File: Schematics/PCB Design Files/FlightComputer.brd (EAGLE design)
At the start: 50.5 x 101.6 mm, 9 parts

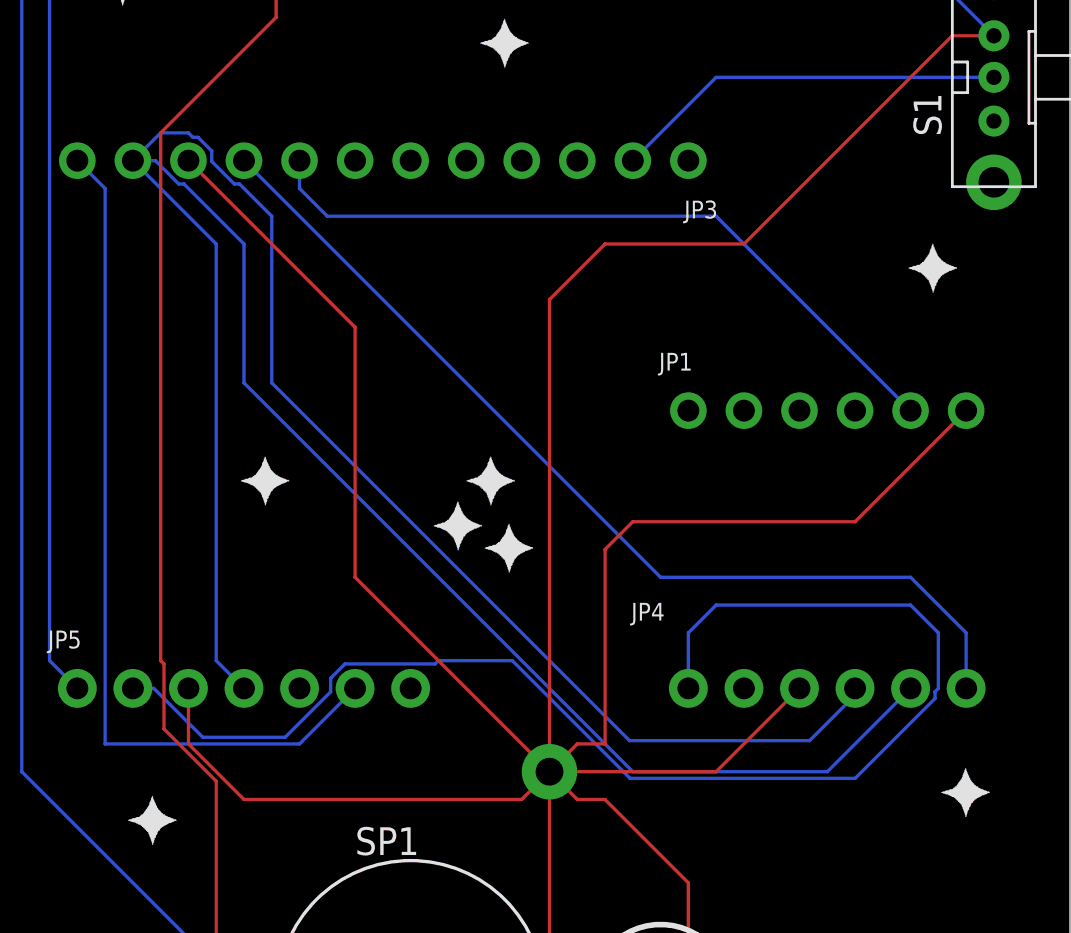
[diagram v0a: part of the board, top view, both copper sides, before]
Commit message: Created header files for simplicity and abstracted code for cleanliness
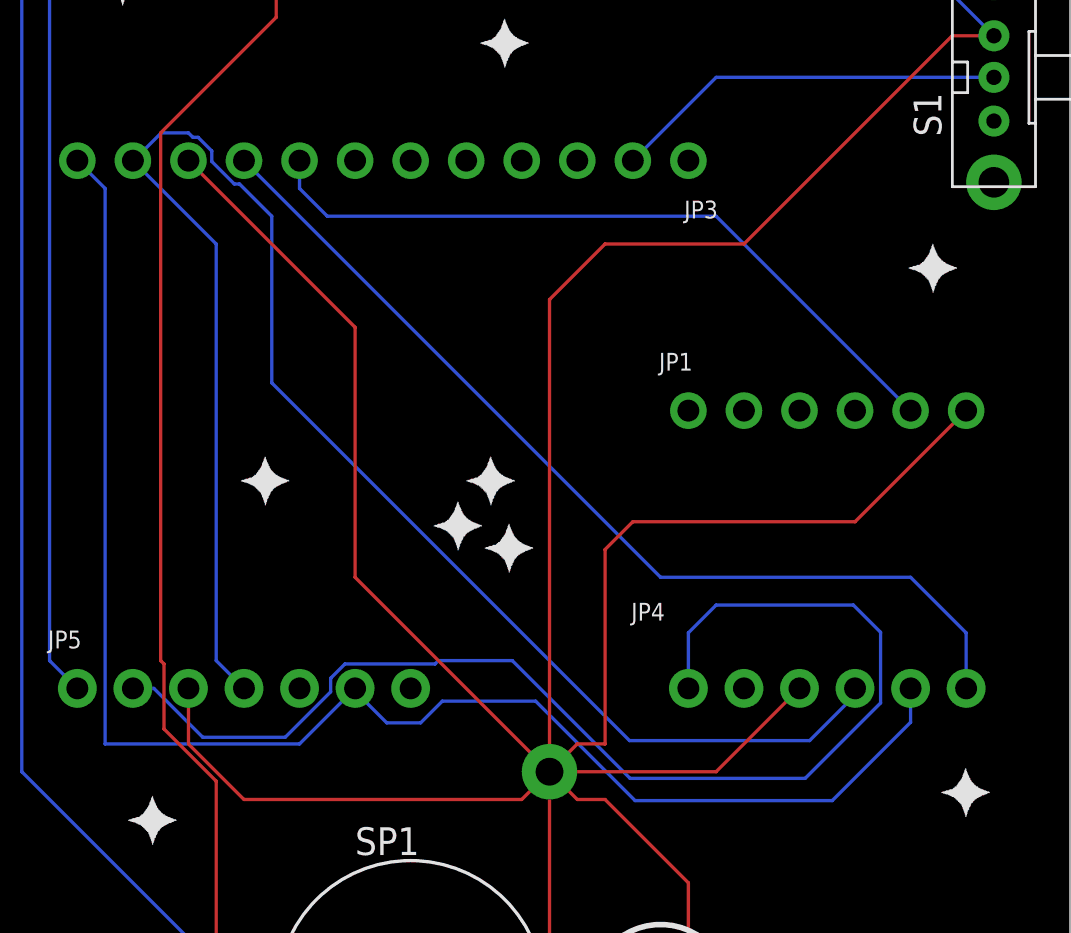
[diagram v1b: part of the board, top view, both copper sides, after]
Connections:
- net SCL: no longer JP4.5
- net SDA: now also JP4.5
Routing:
- net SCL: track 129.6 -> 77.2 mm
- net SDA: track 39.7 -> 71.1 mm
- net 3.3V: track 61.3 -> 56.2 mm
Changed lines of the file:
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@@
 <drawing>
 <settings>
-<setting alwaysvectorfont="yes"/>
+<setting alwaysvectorfont="no"/>
 <setting verticaltext="up"/>
 </settings>
@@
 <contactref element="JP5" pad="4"/>
 <contactref element="JP3" pad="11"/>
-<contactref element="JP4" pad="5"/>
 <wire x1="29.21" y1="57.15" x2="33.02" y2="53.34" width="0.1524" layer="16"/>
 <wire x1="33.02" y1="34.29" x2="34.29" y2="33.02" width="0.1524" layer="16"/>
 <wire x1="33.02" y1="53.34" x2="33.02" y2="34.29" width="0.1524" layer="16"/>
-<wire x1="64.77" y1="33.02" x2="60.96" y2="29.21" width="0.1524" layer="16"/>
-<wire x1="34.29" y1="46.99" x2="34.29" y2="53.34" width="0.1524" layer="16"/>
-<wire x1="34.29" y1="53.34" x2="31.5468" y2="56.0832" width="0.1524" layer="16"/>
-<wire x1="31.5468" y1="56.0832" x2="31.3081125" y2="56.0832" width="0.1524" layer="16"/>
-<wire x1="30.2413125" y1="57.15" x2="29.21" y2="57.15" width="0.1524" layer="16"/>
-<wire x1="31.3081125" y1="56.0832" x2="30.2413125" y2="57.15" width="0.1524" layer="16"/>
-<wire x1="60.96" y1="29.21" x2="52.07" y2="29.21" width="0.1524" layer="16"/>
-<wire x1="52.07" y1="29.21" x2="34.29" y2="46.99" width="0.1524" layer="16"/>
 <wire x1="62.23" y1="33.02" x2="62.23" y2="32.70946875" width="0.1524" layer="16"/>
 <wire x1="62.23" y1="32.70946875" x2="60.15293125" y2="30.6324" width="0.1524" layer="16"/>
@@
 <wire x1="33.8481125" y1="56.0832" x2="32.8168" y2="57.1145125" width="0.1524" layer="16"/>
 <wire x1="32.8168" y1="57.1145125" x2="32.8168" y2="57.5918875" width="0.1524" layer="16"/>
-<wire x1="31.75" y1="58.42" x2="30.48" y2="58.42" width="0.1524" layer="16"/>
-<wire x1="30.48" y1="58.42" x2="29.21" y2="57.15" width="0.1524" layer="16"/>
+<wire x1="31.75" y1="58.42" x2="30.5054" y2="58.42" width="0.1524" layer="16"/>
+<wire x1="30.5054" y1="58.42" x2="29.2354" y2="57.15" width="0.1524" layer="16"/>
+<wire x1="29.2354" y1="57.15" x2="29.21" y2="57.15" width="0.1524" layer="16"/>
 </signal>
 <signal name="SDA">
@@
 <wire x1="27.94" y1="30.48" x2="36.83" y2="30.48" width="0.1524" layer="16"/>
 <wire x1="36.83" y1="30.48" x2="39.37" y2="33.02" width="0.1524" layer="16"/>
+<wire x1="61.1886" y1="27.8892" x2="64.77" y2="31.4706" width="0.1524" layer="16"/>
+<wire x1="61.1886" y1="27.8892" x2="52.1716" y2="27.8892" width="0.1524" layer="16"/>
+<wire x1="43.3578" y1="32.4358" x2="42.3672" y2="31.4452" width="0.1524" layer="16"/>
+<wire x1="42.3672" y1="31.4452" x2="40.8178" y2="31.4452" width="0.1524" layer="16"/>
+<wire x1="52.1716" y1="27.8892" x2="47.625" y2="32.4358" width="0.1524" layer="16"/>
+<wire x1="47.625" y1="32.4358" x2="43.3578" y2="32.4358" width="0.1524" layer="16"/>
+<contactref element="JP4" pad="5"/>
+<wire x1="64.77" y1="31.4706" x2="64.77" y2="33.02" width="0.1524" layer="16"/>
+<wire x1="39.37" y1="32.893" x2="39.37" y2="33.02" width="0.1524" layer="16"/>
+<wire x1="40.8178" y1="31.4452" x2="39.37" y2="32.893" width="0.1524" layer="16"/>
 </signal>
 <signal name="3.3V">
@@
 <wire x1="43.18" y1="34.29" x2="46.55894375" y2="34.29" width="0.1524" layer="16"/>
 <wire x1="46.55894375" y1="34.29" x2="51.94374375" y2="28.9052" width="0.1524" layer="16"/>
-<wire x1="65.8876" y1="32.55706875" x2="65.8876" y2="32.8676" width="0.1524" layer="16"/>
-<wire x1="65.8876" y1="32.8676" x2="66.04" y2="33.02" width="0.1524" layer="16"/>
-<wire x1="51.94374375" y1="28.9052" x2="62.23573125" y2="28.9052" width="0.1524" layer="16"/>
-<wire x1="62.23573125" y1="28.9052" x2="65.8876" y2="32.55706875" width="0.1524" layer="16"/>
-<wire x1="66.04" y1="33.02" x2="66.04" y2="35.56" width="0.1524" layer="16"/>
-<wire x1="66.04" y1="35.56" x2="64.77" y2="36.83" width="0.1524" layer="16"/>
-<wire x1="64.77" y1="36.83" x2="55.88" y2="36.83" width="0.1524" layer="16"/>
+<wire x1="51.94374375" y1="28.9052" x2="59.94973125" y2="28.9052" width="0.1524" layer="16"/>
+<wire x1="63.3984" y1="32.35386875" x2="59.94973125" y2="28.9052" width="0.1524" layer="16"/>
+<wire x1="55.88" y1="36.83" x2="62.1538" y2="36.83" width="0.1524" layer="16"/>
 <wire x1="55.88" y1="36.83" x2="54.61" y2="35.56" width="0.1524" layer="16"/>
 <wire x1="54.61" y1="35.56" x2="54.61" y2="33.02" width="0.1524" layer="16"/>
+<wire x1="63.3984" y1="35.5854" x2="63.3984" y2="32.35386875" width="0.1524" layer="16"/>
+<wire x1="62.1538" y1="36.83" x2="63.3984" y2="35.5854" width="0.1524" layer="16"/>
 </signal>
 <signal name="INT">
